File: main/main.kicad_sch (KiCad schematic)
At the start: 5 parts, among them SW1 SW_DPST_x2

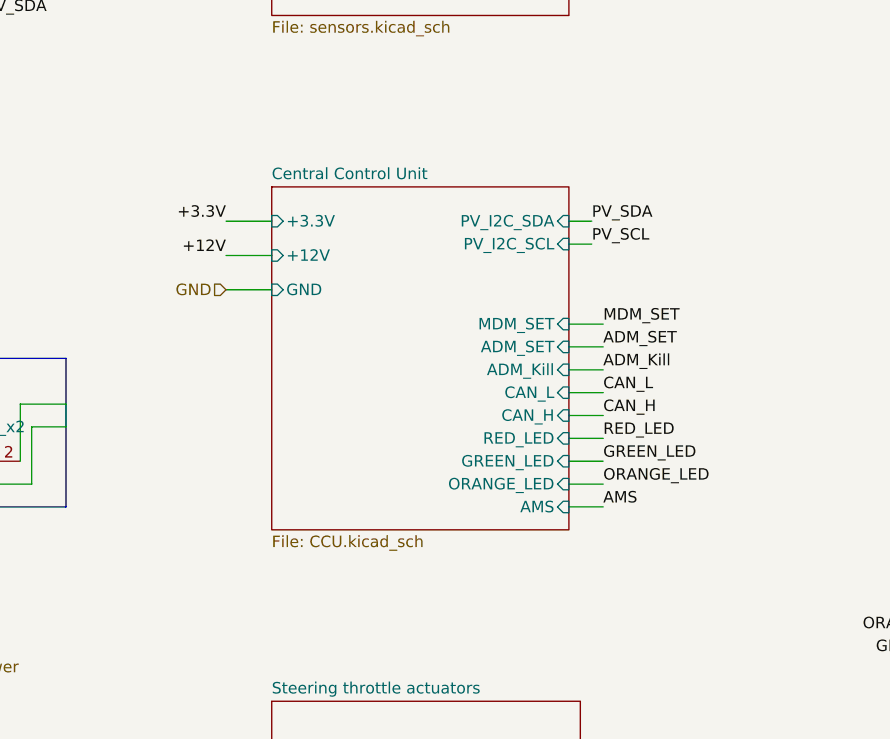
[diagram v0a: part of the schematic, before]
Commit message: added new sheet (switching system), created a few new symbols, changed +48V coming from battery to Battery_High_voltage, added new flags: -ADM_SET, - MDM_SET, -ADM_KILL, -Batt_HIGH_voltage. Erased previous emergency switches.
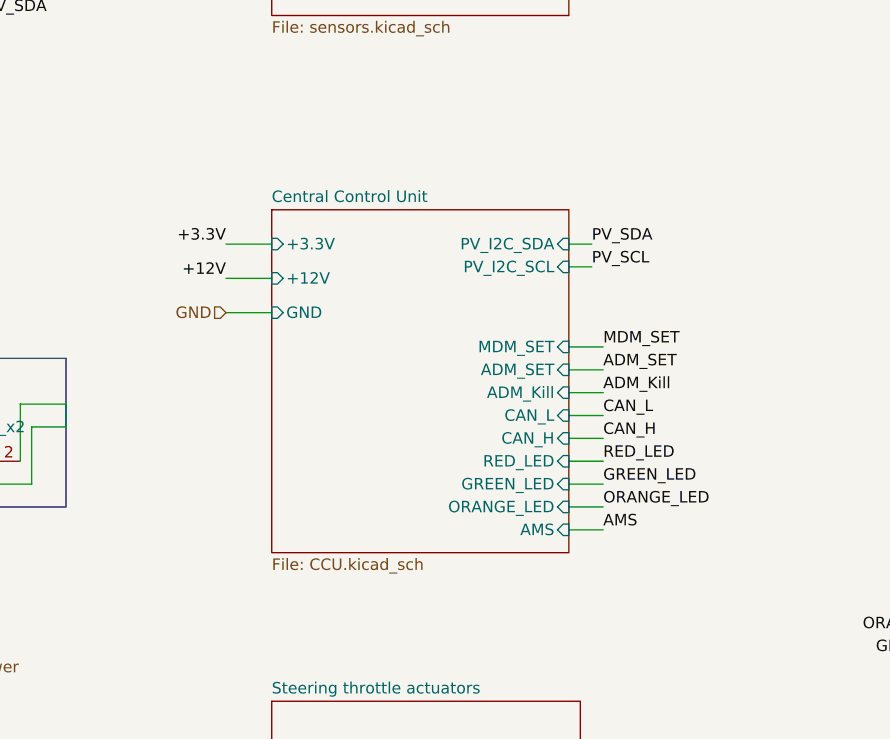
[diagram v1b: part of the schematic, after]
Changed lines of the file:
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@@
 	(wire
 		(pts
-			(xy 152.4 81.28) (xy 156.21 81.28)
+			(xy 152.4 83.82) (xy 156.21 83.82)
 		)
 		(stroke
@@
 	(wire
 		(pts
-			(xy 152.4 76.2) (xy 156.21 76.2)
+			(xy 152.4 78.74) (xy 156.21 78.74)
 		)
 		(stroke
@@
 	(wire
 		(pts
-			(xy 152.4 96.52) (xy 156.21 96.52)
+			(xy 152.4 99.06) (xy 156.21 99.06)
 		)
 		(stroke
@@
 	(wire
 		(pts
-			(xy 114.3 72.39) (xy 119.38 72.39)
+			(xy 114.3 74.93) (xy 119.38 74.93)
 		)
 		(stroke
@@
 	(wire
 		(pts
-			(xy 152.4 86.36) (xy 156.21 86.36)
+			(xy 152.4 88.9) (xy 156.21 88.9)
 		)
 		(stroke
@@
 	(wire
 		(pts
-			(xy 152.4 88.9) (xy 156.21 88.9)
+			(xy 152.4 91.44) (xy 156.21 91.44)
 		)
 		(stroke
@@
 	(wire
 		(pts
-			(xy 152.4 64.77) (xy 154.94 64.77)
+			(xy 152.4 67.31) (xy 154.94 67.31)
 		)
 		(stroke
@@
 	(wire
 		(pts
-			(xy 152.4 78.74) (xy 156.21 78.74)
+			(xy 152.4 81.28) (xy 156.21 81.28)
 		)
 		(stroke
@@
 	(wire
 		(pts
-			(xy 119.38 64.77) (xy 114.3 64.77)
+			(xy 119.38 67.31) (xy 114.3 67.31)
 		)
 		(stroke
@@
 	(wire
 		(pts
-			(xy 152.4 91.44) (xy 156.21 91.44)
+			(xy 152.4 93.98) (xy 156.21 93.98)
 		)
 		(stroke
@@
 	(wire
 		(pts
-			(xy 152.4 93.98) (xy 156.21 93.98)
+			(xy 152.4 96.52) (xy 156.21 96.52)
 		)
 		(stroke
@@
 	(wire
 		(pts
-			(xy 114.3 68.58) (xy 119.38 68.58)
+			(xy 114.3 71.12) (xy 119.38 71.12)
 		)
 		(stroke
@@
 	(wire
 		(pts
-			(xy 152.4 67.31) (xy 154.94 67.31)
+			(xy 152.4 69.85) (xy 154.94 69.85)
 		)
 		(stroke
@@
 	(wire
 		(pts
-			(xy 152.4 83.82) (xy 156.21 83.82)
+			(xy 152.4 86.36) (xy 156.21 86.36)
 		)
 		(stroke
@@
 	)
 	(label "ORANGE_LED"
-		(at 156.21 93.98 0)
+		(at 156.21 96.52 0)
 		(fields_autoplaced yes)
 		(effects
@@
 	)
 	(label "AMS"
-		(at 156.21 96.52 0)
+		(at 156.21 99.06 0)
 		(fields_autoplaced yes)
 		(effects
@@
 	)
 	(label "RED_LED"
-		(at 156.21 88.9 0)
+		(at 156.21 91.44 0)
 		(fields_autoplaced yes)
 		(effects
@@
 	)
 	(label "CAN_H"
-		(at 156.21 86.36 0)
+		(at 156.21 88.9 0)
 		(fields_autoplaced yes)
 		(effects
@@
 	)
 	(label "ADM_SET"
-		(at 156.21 78.74 0)
+		(at 156.21 81.28 0)
 		(fields_autoplaced yes)
 		(effects
@@
 	)
 	(label "GREEN_LED"
-		(at 156.21 91.44 0)
+		(at 156.21 93.98 0)
 		(fields_autoplaced yes)
 		(effects
@@
 	)
 	(label "PV_SDA"
-		(at 154.94 64.77 0)
+		(at 154.94 67.31 0)
 		(fields_autoplaced yes)
 		(effects
@@
 	)
 	(label "+12V"
-		(at 114.3 68.58 180)
+		(at 114.3 71.12 180)
 		(fields_autoplaced yes)
 		(effects
@@
 	)
 	(label "+3.3V"
-		(at 114.3 64.77 180)
+		(at 114.3 67.31 180)
 		(fields_autoplaced yes)
 		(effects
@@
 	)
 	(label "ADM_Kill"
-		(at 156.21 81.28 0)
+		(at 156.21 83.82 0)
 		(fields_autoplaced yes)
 		(effects
@@
 	)
 	(label "CAN_L"
-		(at 156.21 83.82 0)
+		(at 156.21 86.36 0)
 		(fields_autoplaced yes)
 		(effects
@@
 	)
 	(label "PV_SCL"
-		(at 154.94 67.31 0)
+		(at 154.94 69.85 0)
 		(fields_autoplaced yes)
 		(effects
@@
 	)
 	(label "MDM_SET"
-		(at 156.21 76.2 0)
+		(at 156.21 78.74 0)
 		(fields_autoplaced yes)
 		(effects
@@
 	(hierarchical_label "GND"
 		(shape input)
-		(at 114.3 72.39 180)
+		(at 114.3 74.93 180)
 		(fields_autoplaced yes)
 		(effects
@@
 	)
 	(sheet
-		(at 119.38 60.96)
+		(at 119.38 63.5)
 		(size 33.02 38.1)
 		(fields_autoplaced yes)
@@
 		)
 		(property "Sheetname" "Central Control Unit"
-			(at 119.38 60.2484 0)
+			(at 119.38 62.7884 0)
 			(effects
 				(font
@@
 		)
 		(property "Sheetfile" "CCU.kicad_sch"
-			(at 119.38 99.6446 0)
+			(at 119.38 102.1846 0)
 			(effects
 				(font
@@
 		)
 		(pin "GND" input
-			(at 119.38 72.39 180)
+			(at 119.38 74.93 180)
 			(effects
 				(font
@@
 		)
 		(pin "+12V" input
-			(at 119.38 68.58 180)
+			(at 119.38 71.12 180)
 			(effects
 				(font
@@
 		)
 		(pin "PV_I2C_SDA" input
-			(at 152.4 64.77 0)
+			(at 152.4 67.31 0)
 			(effects
 				(font
@@
 		)
 		(pin "PV_I2C_SCL" input
-			(at 152.4 67.31 0)
+			(at 152.4 69.85 0)
 			(effects
 				(font
@@
 		)
 		(pin "+3.3V" input
-			(at 119.38 64.77 180)
+			(at 119.38 67.31 180)
 			(effects
 				(font
@@
 		)
 		(pin "CAN_L" input
-			(at 152.4 83.82 0)
+			(at 152.4 86.36 0)
 			(effects
 				(font
@@
 		)
 		(pin "CAN_H" input
-			(at 152.4 86.36 0)
+			(at 152.4 88.9 0)
 			(effects
 				(font
@@
 		)
 		(pin "RED_LED" input
-			(at 152.4 88.9 0)
+			(at 152.4 91.44 0)
 			(effects
 				(font
@@
 		)
 		(pin "GREEN_LED" input
-			(at 152.4 91.44 0)
+			(at 152.4 93.98 0)
 			(effects
 				(font
@@
 		)
 		(pin "ORANGE_LED" input
-			(at 152.4 93.98 0)
+			(at 152.4 96.52 0)
 			(effects
 				(font
@@
 		)
 		(pin "AMS" input
-			(at 152.4 96.52 0)
+			(at 152.4 99.06 0)
 			(effects
 				(font
@@
 		)
 		(pin "ADM_Kill" input
-			(at 152.4 81.28 0)
+			(at 152.4 83.82 0)
 			(effects
 				(font
@@
 		)
 		(pin "ADM_SET" input
-			(at 152.4 78.74 0)
+			(at 152.4 81.28 0)
 			(effects
 				(font
@@
 		)
 		(pin "MDM_SET" input
-			(at 152.4 76.2 0)
+			(at 152.4 78.74 0)
 			(effects
 				(font

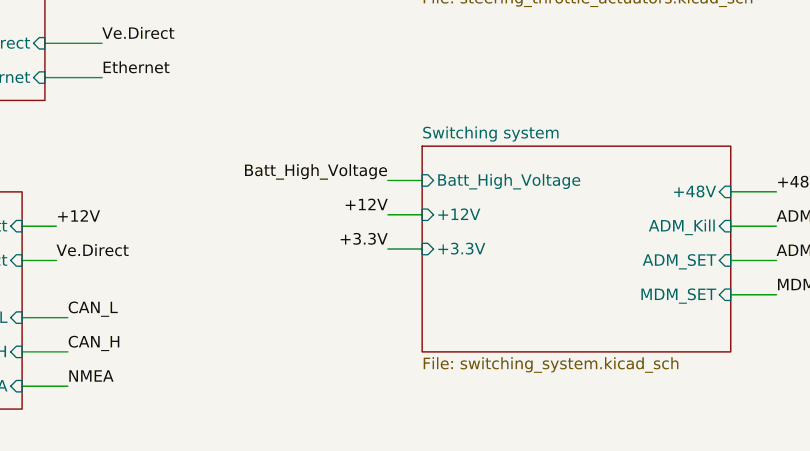
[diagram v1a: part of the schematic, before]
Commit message: added GND pin to switching system sheet
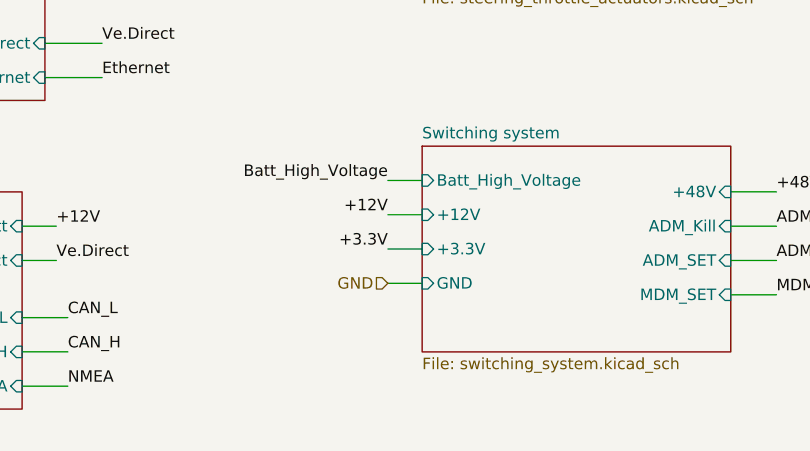
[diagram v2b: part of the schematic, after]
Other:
- sheet Switching system ports: added GND; removed none
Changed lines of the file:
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@@
 	(wire
 		(pts
+			(xy 115.57 170.18) (xy 119.38 170.18)
+		)
+		(stroke
+			(width 0)
+			(type default)
+		)
+	)
+	(wire
+		(pts
 			(xy 40.64 31.75) (xy 43.18 31.75)
 		)
@@
 	(hierarchical_label "GND"
 		(shape input)
+		(at 115.57 170.18 180)
+		(fields_autoplaced yes)
+		(effects
+			(font
+				(size 1.27 1.27)
+			)
+			(justify right)
+		)
+	)
+	(hierarchical_label "GND"
+		(shape input)
 		(at 52.07 68.58 180)
 		(fields_autoplaced yes)
@@
 			)
 		)
+		(pin "GND" input
+			(at 119.38 170.18 180)
+			(effects
+				(font
+					(size 1.27 1.27)
+				)
+				(justify left)
+			)
+		)

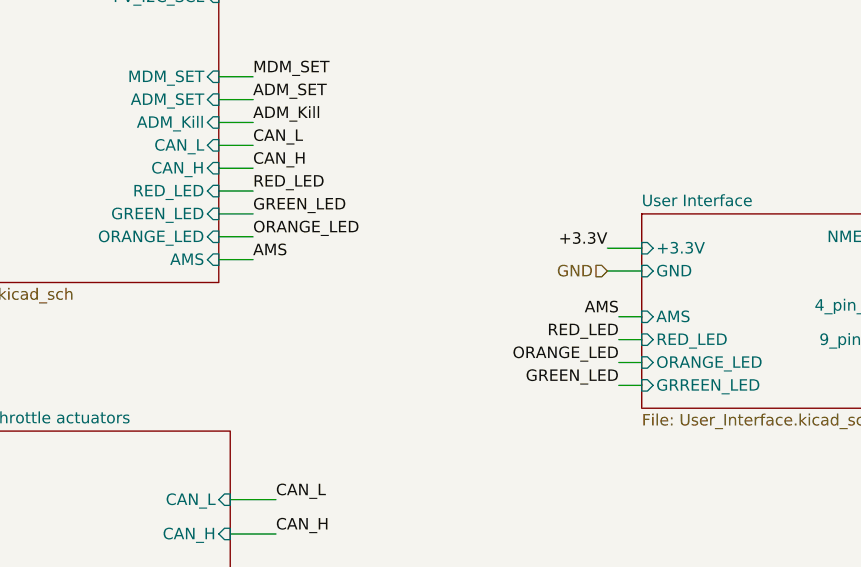
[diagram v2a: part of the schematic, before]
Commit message: removed AMS line, and previous switch ing UI. Renamed Switch in switching system to AMS
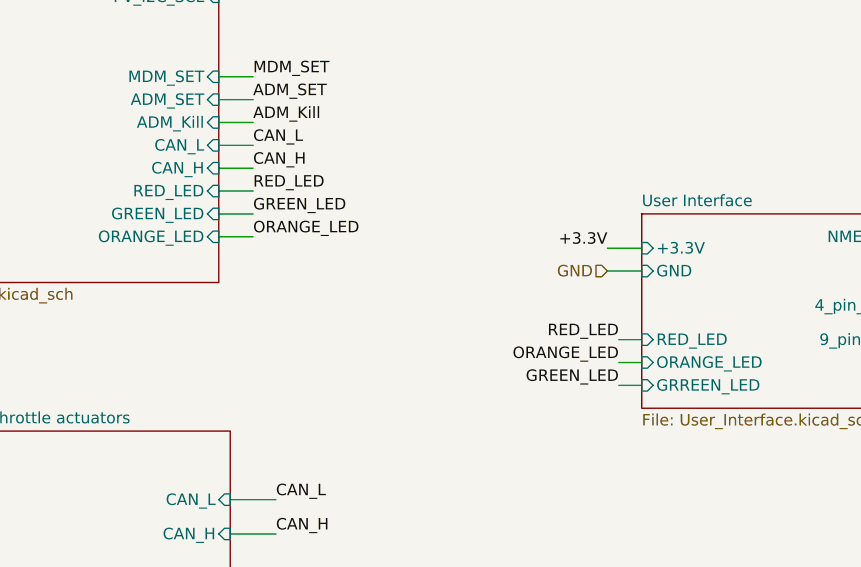
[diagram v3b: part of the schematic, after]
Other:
- sheet Central Control Unit ports: added none; removed AMS
- sheet User Interface ports: added none; removed AMS
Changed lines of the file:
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@@
 	(wire
 		(pts
-			(xy 152.4 99.06) (xy 156.21 99.06)
-		)
-		(stroke
-			(width 0)
-			(type default)
-		)
-	)
-	(wire
-		(pts
 			(xy 85.09 33.02) (xy 83.82 33.02)
 		)
@@
 	(wire
 		(pts
-			(xy 196.85 105.41) (xy 199.39 105.41)
-		)
-		(stroke
-			(width 0)
-			(type default)
-		)
-	)
-	(wire
-		(pts
 			(xy 153.67 125.73) (xy 158.75 125.73)
 		)
@@
 		)
 	)
-	(label "AMS"
-		(at 156.21 99.06 0)
-		(fields_autoplaced yes)
-		(effects
-			(font
-				(size 1.27 1.27)
-			)
-			(justify left bottom)
-		)
-	)
 	(label "RED_LED"
 		(at 156.21 91.44 0)
@@
 		)
 	)
-	(label "AMS"
-		(at 196.85 105.41 180)
-		(fields_autoplaced yes)
-		(effects
-			(font
-				(size 1.27 1.27)
-			)
-			(justify right bottom)
-		)
-	)
 	(label "4_pin_power"
 		(at 238.76 104.14 0)
@@
 			)
 		)
-		(pin "AMS" input
-			(at 152.4 99.06 0)
-			(effects
-				(font
-					(size 1.27 1.27)
-				)
-				(justify right)
-			)
-		)
 		(pin "ADM_Kill" input
 			(at 152.4 83.82 0)
@@
 			(effects
 				(font
-					(size 1.27 1.27)
-				)
-				(justify left)
-			)
-		)
-		(pin "AMS" input
-			(at 199.39 105.41 180)
-			(effects
-				(font

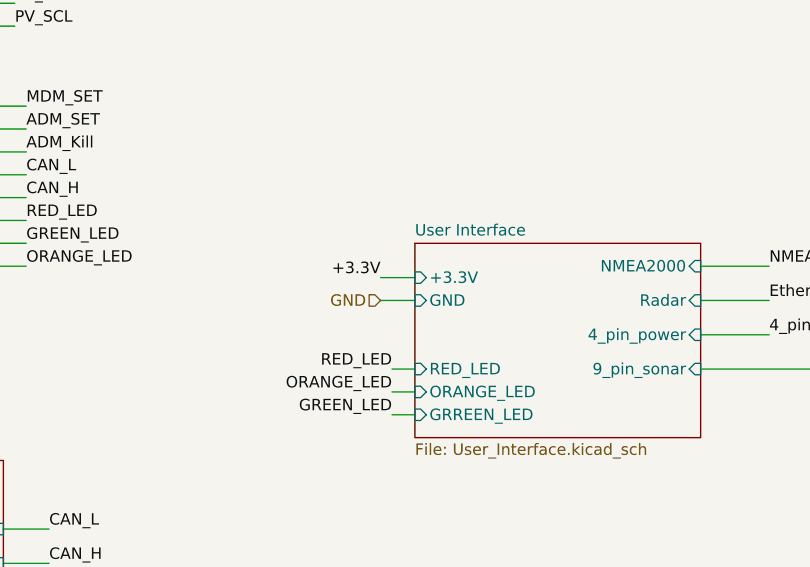
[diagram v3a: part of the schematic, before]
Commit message: Removed +3.3V connected to UI
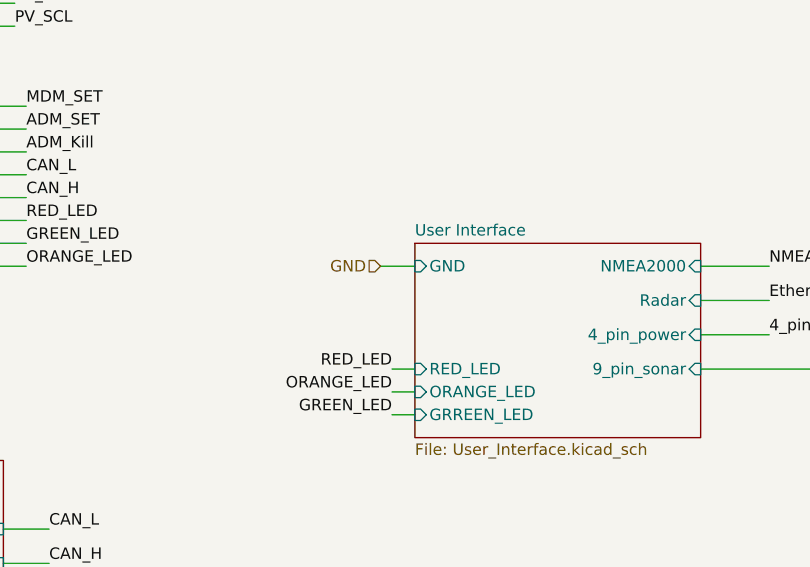
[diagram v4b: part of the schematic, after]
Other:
- sheet User Interface ports: added none; removed +3.3V
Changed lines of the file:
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@@
 	(wire
 		(pts
-			(xy 195.58 100.33) (xy 199.39 100.33)
+			(xy 195.58 96.52) (xy 199.39 96.52)
 		)
 		(stroke
@@
 	(wire
 		(pts
-			(xy 195.58 97.79) (xy 199.39 97.79)
-		)
-		(stroke
-			(width 0)
-			(type default)
-		)
-	)
-	(wire
-		(pts
 			(xy 114.3 71.12) (xy 119.38 71.12)
 		)
@@
 		)
 	)
-	(label "+3.3V"
-		(at 195.58 97.79 180)
-		(fields_autoplaced yes)
-		(effects
-			(font
-				(size 1.27 1.27)
-			)
-			(justify right bottom)
-		)
-	)
 	(label "VCC_PV"
 		(at 40.64 31.75 180)
@@
 	(hierarchical_label "GND"
 		(shape input)
-		(at 195.58 100.33 180)
+		(at 195.58 96.52 180)
 		(fields_autoplaced yes)
 		(effects
@@
 			)
 		)
-		(pin "+3.3V" input
-			(at 199.39 97.79 180)
-			(effects
-				(font
-					(size 1.27 1.27)
-				)
-				(justify left)
-			)
-		)
 		(pin "GND" input
-			(at 199.39 100.33 180)
+			(at 199.39 96.52 180)
 			(effects
 				(font
